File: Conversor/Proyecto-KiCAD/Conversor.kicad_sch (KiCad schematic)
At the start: 25 parts, among them J2 ConnPila, J3 ConnTrafoP, J4 ConnTrafoS, J5 ConnLf, J6 ConnCarga, Q1 IRFP150, Q2 IRFP150, Q3 IRFP150, Q4 IRFP150

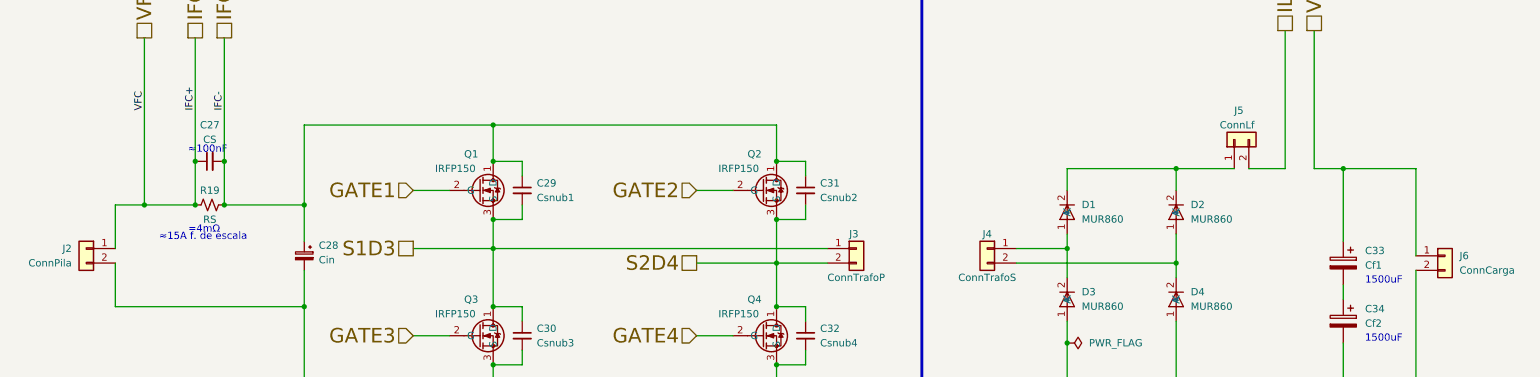
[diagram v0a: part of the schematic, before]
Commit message: Progresar con los recomendaciones de Claus
- Arreglar resistencia shunt y pistas de alimentación
- Cambiados los simbolos de conectores de trafo, pila, inductor y carga
por screw terminals, todavía no está actualizado en la PCB
- Tambien terminar de ver las layout recommendations
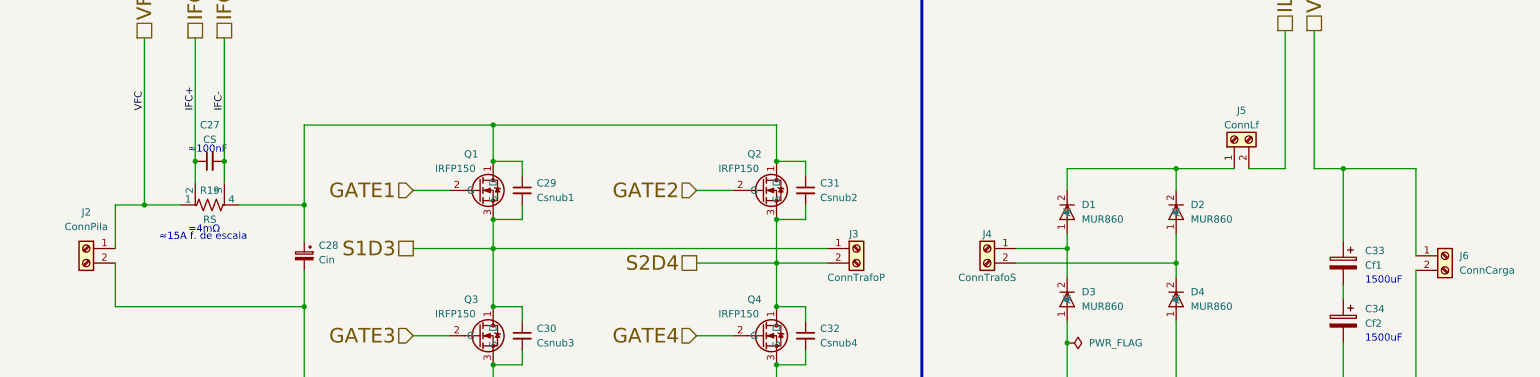
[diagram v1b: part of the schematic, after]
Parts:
- removed J2: ConnPila, TerminalBlock:TerminalBlock_Wuerth_691311400102_P7.62mm, symbol Connector_Generic:Conn_01x02
- removed J3: ConnTrafoP, TerminalBlock:TerminalBlock_Wuerth_691311400102_P7.62mm, symbol Connector_Generic:Conn_01x02
- removed J4: ConnTrafoS, TerminalBlock:TerminalBlock_Wuerth_691311400102_P7.62mm, symbol Connector_Generic:Conn_01x02
- removed J5: ConnLf, TerminalBlock:TerminalBlock_Wuerth_691311400102_P7.62mm, symbol Connector_Generic:Conn_01x02
- removed J6: ConnCarga, TerminalBlock:TerminalBlock_Wuerth_691311400102_P7.62mm, symbol Connector_Generic:Conn_01x02
- removed R19: RS, Resistor_SMD:R_2512_6332Metric_Pad1.40x3.35mm_HandSolder, symbol Device:R_Small_US
- added J2: ConnPila, symbol Connector:Screw_Terminal_01x02
- added J3: ConnTrafoP, symbol Connector:Screw_Terminal_01x02
- added J4: ConnTrafoS, symbol Connector:Screw_Terminal_01x02
- added J5: ConnLf, symbol Connector:Screw_Terminal_01x02
- added J6: ConnCarga, symbol Connector:Screw_Terminal_01x02
- added R19: RS, Resistor_SMD:R_Shunt_Vishay_WSK2512_6332Metric_T2.21mm, symbol Device:R_Shunt_US
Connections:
- net GND1: now also J2.2 (Pin_2)
- net GND2: now also J6.2 (Pin_2)
- net IFC+: now also R19.2
- net IFC-: now also R19.3; no longer C28.1, C29.1, C31.1, Q1.1 (D), Q2.1 (D)
- net ILF+: now also J5.2 (Pin_2)
- net S1D3: now also J3.1 (Pin_1)
- net S2D4: now also J3.2 (Pin_2)
- net VLOAD/ILF-: now also J6.1 (Pin_1)
- net at D1.1 (A), D3.2 (K): now also J4.1 (Pin_1)
- net at D1.2 (K), D2.2 (K): now also J5.1 (Pin_1)
- net at D2.1 (A), D4.2 (K): now also J4.2 (Pin_2)
- new net: C28.1, C29.1, C31.1, Q1.1 (D), Q2.1 (D), R19.4
- new net VFC: J2.1 (Pin_1), R19.1

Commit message: Cambiar los conectores de trafo, inductor, pila y carga
- Por hacer:
  - Cambiar el 12V HD por el conector que mostró Claus
  - Ver las layout recommendations de los reguladores lineales
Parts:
- J2, J3, J4, J5, J6: footprint (none) -> DegsonScrewTerminal:Degson_Screw_Terminal_block_01x02
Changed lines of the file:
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@@
       (effects (font (size 1.27 1.27)) (justify left))
     )
-    (property "Footprint" "" (id 2) (at 167.64 97.79 0)
+    (property "Footprint" "DegsonScrewTerminal:Degson_Screw_Terminal_block_01x02" (id 2) (at 167.64 97.79 0)
       (effects (font (size 1.27 1.27)) hide)
     )
@@
     (property "Reference" "J4" (id 0) (at 190.5 95.25 0))
     (property "Value" "ConnTrafoS" (id 1) (at 190.5 102.87 0))
-    (property "Footprint" "" (id 2) (at 190.5 97.79 0)
+    (property "Footprint" "DegsonScrewTerminal:Degson_Screw_Terminal_block_01x02" (id 2) (at 190.5 97.79 0)
       (effects (font (size 1.27 1.27)) hide)
     )
@@
     (property "Reference" "J2" (id 0) (at 33.02 91.44 0))
     (property "Value" "ConnPila" (id 1) (at 33.02 93.98 0))
-    (property "Footprint" "" (id 2) (at 33.02 97.79 0)
+    (property "Footprint" "DegsonScrewTerminal:Degson_Screw_Terminal_block_01x02" (id 2) (at 33.02 97.79 0)
       (effects (font (size 1.27 1.27)) hide)
     )
@@
       (effects (font (size 1.27 1.27)) (justify left))
     )
-    (property "Footprint" "" (id 2) (at 270.51 99.06 0)
+    (property "Footprint" "DegsonScrewTerminal:Degson_Screw_Terminal_block_01x02" (id 2) (at 270.51 99.06 0)
       (effects (font (size 1.27 1.27)) hide)
     )
@@
     (property "Reference" "J5" (id 0) (at 234.95 73.66 90))
     (property "Value" "ConnLf" (id 1) (at 234.95 76.2 90))
-    (property "Footprint" "" (id 2) (at 233.68 78.74 0)
-      (effects (font (size 1.27 1.27)) hide)
-    )
+    (property "Footprint" "DegsonScrewTerminal:Degson_Screw_Terminal_block_01x02" (id 2) (at 233.68 78.74 0)
+      (effects (font (size 1.27 1.27)) hide)
+    )

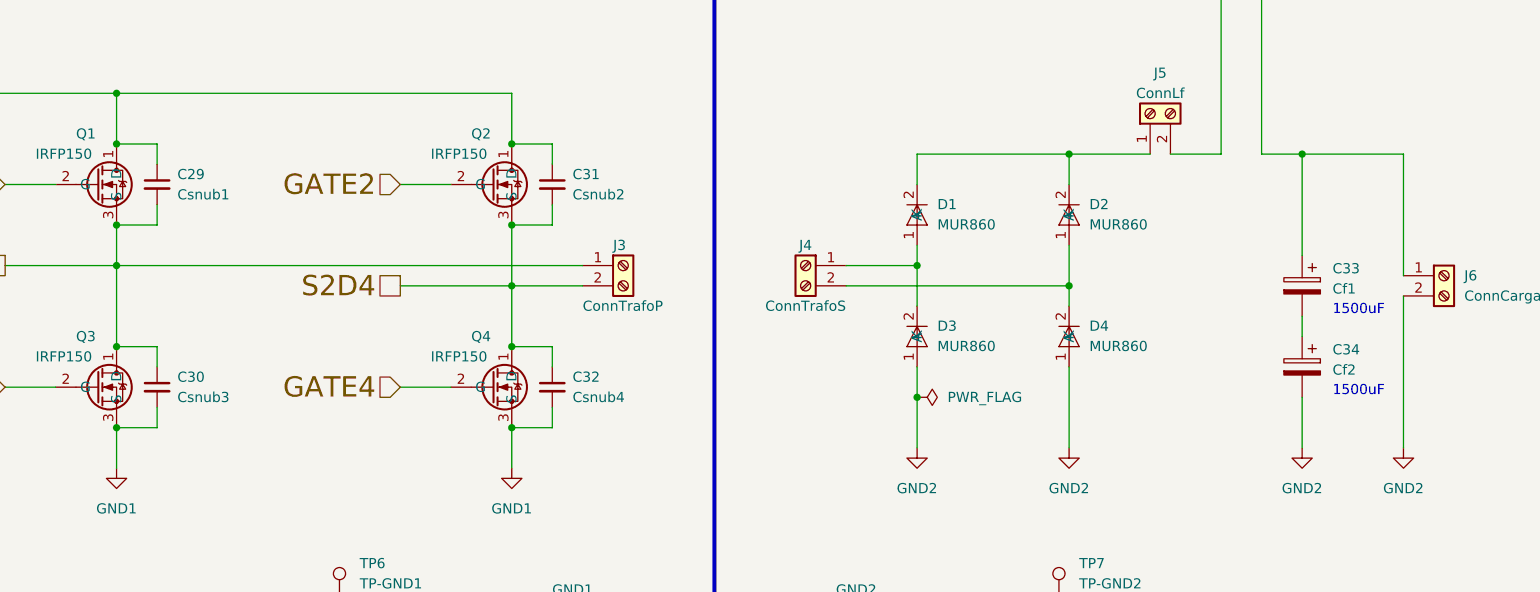
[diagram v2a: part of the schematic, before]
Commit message: Empezar con lar recomendaciones de Jorge
- Agregar nota que contiene todas las recomendaciones (ticks en las que
ya hice)
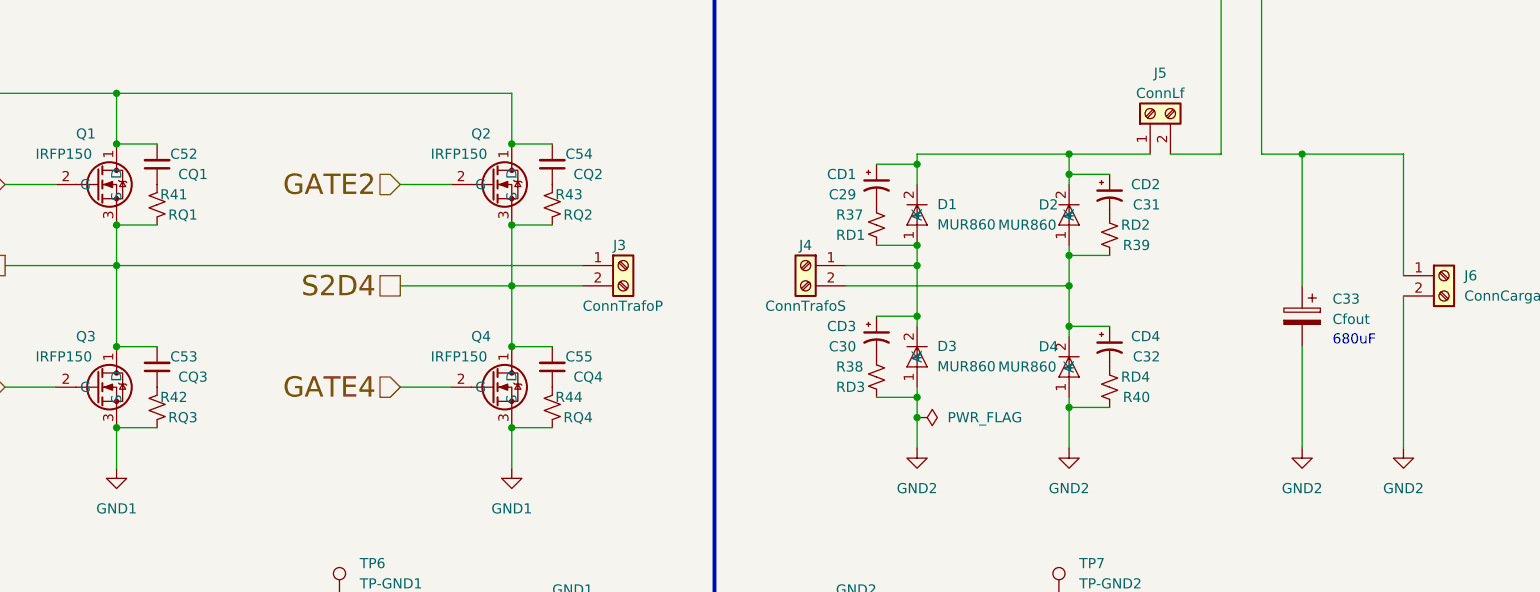
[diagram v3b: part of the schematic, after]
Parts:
- removed C29: Csnub1, Capacitor_SMD:C_1206_3216Metric_Pad1.33x1.80mm_HandSolder, symbol Device:C_Small
- removed C30: Csnub3, Capacitor_SMD:C_1206_3216Metric_Pad1.33x1.80mm_HandSolder, symbol Device:C_Small
- removed C31: Csnub2, Capacitor_SMD:C_1206_3216Metric_Pad1.33x1.80mm_HandSolder, symbol Device:C_Small
- removed C34: Cf2, Capacitor_THT:CP_Radial_D18.0mm_P7.50mm, symbol Device:C_Polarized
- added C30: CD3, Capacitor_THT:CP_Radial_Tantal_D4.5mm_P2.50mm, symbol Device:C_Polarized_Small_US
- added C31: CD2, Capacitor_THT:CP_Radial_Tantal_D4.5mm_P2.50mm, symbol Device:C_Polarized_Small_US
- added C32: CD4, Capacitor_THT:CP_Radial_Tantal_D4.5mm_P2.50mm, symbol Device:C_Polarized_Small_US
- added C52: CQ1, Capacitor_SMD:C_1206_3216Metric_Pad1.33x1.80mm_HandSolder, symbol Device:C_Small
- added C53: CQ3, Capacitor_SMD:C_1206_3216Metric_Pad1.33x1.80mm_HandSolder, symbol Device:C_Small
- added C54: CQ2, Capacitor_SMD:C_1206_3216Metric_Pad1.33x1.80mm_HandSolder, symbol Device:C_Small
- added C55: CQ4, Capacitor_SMD:C_1206_3216Metric_Pad1.33x1.80mm_HandSolder, symbol Device:C_Small
- added R37: RD1, Resistor_THT:R_Axial_DIN0204_L3.6mm_D1.6mm_P5.08mm_Horizontal, symbol Device:R_Small_US
- added R38: RD3, Resistor_THT:R_Axial_DIN0204_L3.6mm_D1.6mm_P5.08mm_Horizontal, symbol Device:R_Small_US
- added R39: RD2, Resistor_THT:R_Axial_DIN0204_L3.6mm_D1.6mm_P5.08mm_Horizontal, symbol Device:R_Small_US
- added R40: RD4, Resistor_THT:R_Axial_DIN0204_L3.6mm_D1.6mm_P5.08mm_Horizontal, symbol Device:R_Small_US
- added R41: RQ1, Resistor_SMD:R_1206_3216Metric_Pad1.30x1.75mm_HandSolder, symbol Device:R_Small_US
- added R42: RQ3, Resistor_SMD:R_1206_3216Metric_Pad1.30x1.75mm_HandSolder, symbol Device:R_Small_US
- added R43: RQ2, Resistor_SMD:R_1206_3216Metric_Pad1.30x1.75mm_HandSolder, symbol Device:R_Small_US
- added R44: RQ4, Resistor_SMD:R_1206_3216Metric_Pad1.30x1.75mm_HandSolder, symbol Device:R_Small_US
- C29: renamed from C32; value Csnub4 -> CD1; footprint Capacitor_SMD:C_1206_3216Metric_Pad1.33x1.80mm_HandSolder -> Capacitor_THT:CP_Radial_Tantal_D4.5mm_P2.50mm; symbol Device:C_Small -> Device:C_Polarized_Small_US
- C33: value Cf1 -> Cfout; footprint Capacitor_THT:CP_Radial_D18.0mm_P7.50mm -> Capacitor_THT:CP_Radial_D22.0mm_P10.00mm_SnapIn
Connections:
- net GND1: now also R42.1, R44.1; no longer C29.2
- net GND2: now also C33.2, R38.1, R40.2
- net S1D3: now also C53.2, R41.1
- net S2D4: now also C55.2, R43.1; no longer C29.1
- net at C28.1, Q1.1 (D), Q2.1 (D)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: now also C52.2, C54.2
- net at D1.1 (A), D3.2 (K), J4.1 (Pin_1): now also C30.1, R37.1
- net at D2.1 (A), D4.2 (K), J4.2 (Pin_2): now also C32.1, R39.2
- net at D1.2 (K), D2.2 (K), J5.1 (Pin_1): now also C29.1, C31.1
- new net: C30.2, R38.2
- new net: C29.2, R37.2
- new net: C55.1, R44.2
- new net: C53.1, R42.2
- new net: C52.1, R41.2
- new net: C54.1, R43.2
- new net: C31.2, R39.1
- new net: C32.2, R40.1
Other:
- note added: "680uF"
- note removed: "1500uF"
- moved on the sheet: C33, D3, D4

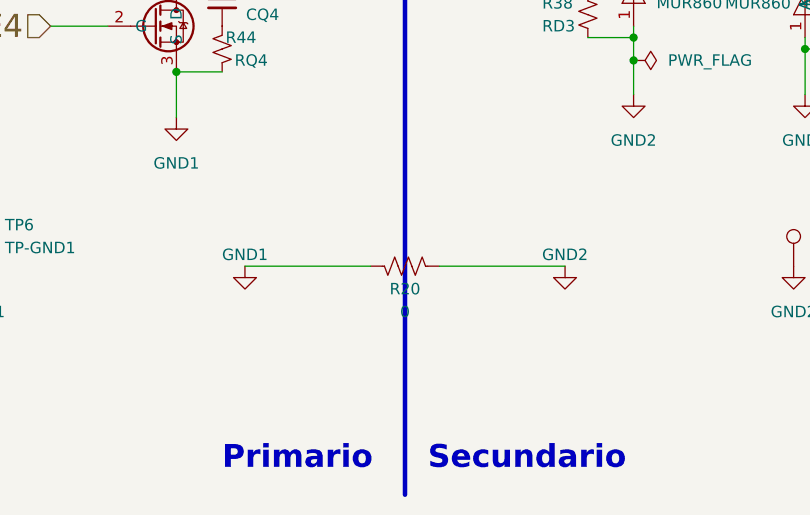
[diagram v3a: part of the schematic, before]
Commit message: Corregir las cosas que me indico Jorge
- Por hacer:
  - Verificar las correcciones con Jorge
  - Ver si se consigue un capacitor mas chico (~20mm) para la entrada
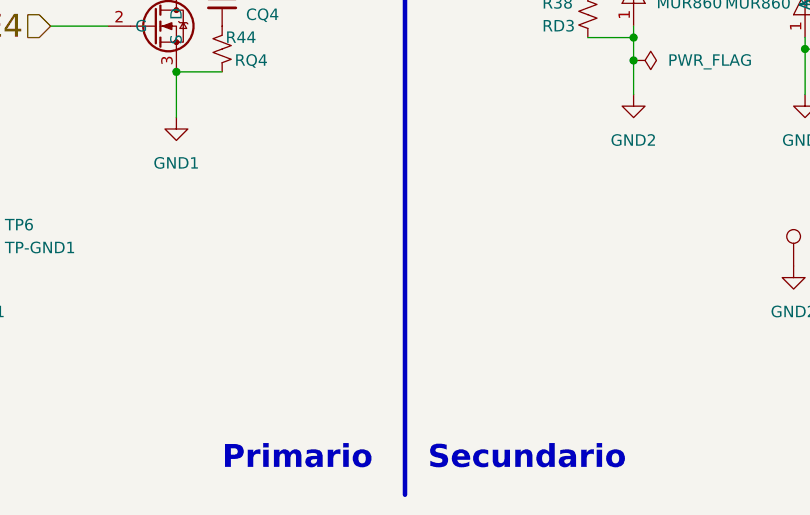
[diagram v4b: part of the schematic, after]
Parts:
- removed R20: 0, Resistor_SMD:R_1206_3216Metric_Pad1.30x1.75mm_HandSolder, symbol Device:R_US
- C28: footprint Capacitor_THT:CP_Radial_D12.5mm_P5.00mm -> Capacitor_THT:CP_Radial_D22.0mm_P10.00mm_SnapIn
- C33: footprint Capacitor_THT:CP_Radial_D22.0mm_P10.00mm_SnapIn -> Capacitor_THT:CP_Radial_D25.0mm_P10.00mm_SnapIn
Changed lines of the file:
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@@
-    (stroke (width 0) (type default) (color 0 0 0 0))
-  )
-  (wire (pts (xy 175.26 139.7) (xy 161.29 139.7))
     (stroke (width 0) (type default) (color 0 0 0 0))
   )
@@
   )
   (wire (pts (xy 204.47 116.84) (xy 204.47 120.65))
-    (stroke (width 0) (type default) (color 0 0 0 0))
-  )
-  (wire (pts (xy 196.85 139.7) (xy 182.88 139.7))
     (stroke (width 0) (type default) (color 0 0 0 0))
   )
@@
       (effects (font (size 1.27 1.27)) (justify right))
     )
-    (property "Footprint" "Capacitor_THT:CP_Radial_D12.5mm_P5.00mm" (id 2) (at 71.12 99.06 0)
+    (property "Footprint" "Capacitor_THT:CP_Radial_D22.0mm_P10.00mm_SnapIn" (id 2) (at 71.12 99.06 0)
       (effects (font (size 1.27 1.27)) hide)
     )
@@
     )
     (property "Datasheet" "" (id 3) (at 204.47 92.71 0)
-      (effects (font (size 1.27 1.27)) hide)
-    )
-    (pin "1")
-    (pin "2")
-  )
-  (symbol (lib_id "Device:R_US") (at 179.07 139.7 270) (mirror x) (unit 1)
-    (in_bom yes) (on_board yes)
-    (property "Reference" "R20" (id 0) (at 179.07 142.24 90))
-    (property "Value" "0" (id 1) (at 179.07 144.78 90))
-    (property "Footprint" "Resistor_SMD:R_1206_3216Metric_Pad1.30x1.75mm_HandSolder" (id 2) (at 178.816 138.684 90)
-      (effects (font (size 1.27 1.27)) hide)
-    )
-    (property "Datasheet" "~" (id 3) (at 179.07 139.7 0)
       (effects (font (size 1.27 1.27)) hide)
     )
@@
     (pin "1")
   )
-  (symbol (lib_id "power:GND1") (at 161.29 139.7 0) (mirror y) (unit 1)
-    (in_bom yes) (on_board yes)
-    (property "Reference" "#PWR069" (id 0) (at 161.29 146.05 0)
-      (effects (font (size 1.27 1.27)) hide)
-    )
-    (property "Value" "GND1" (id 1) (at 161.29 138.43 0))
-    (property "Footprint" "" (id 2) (at 161.29 139.7 0)
-      (effects (font (size 1.27 1.27)) hide)
-    )
-    (property "Datasheet" "" (id 3) (at 161.29 139.7 0)
-      (effects (font (size 1.27 1.27)) hide)
-    )
-    (pin "1")
-  )
   (symbol (lib_id "power:GND2") (at 204.47 120.65 0) (unit 1)
     (in_bom yes) (on_board yes) (fields_autoplaced)
@@
     )
     (property "Datasheet" "" (id 3) (at 204.47 120.65 0)
-      (effects (font (size 1.27 1.27)) hide)
-    )
-    (pin "1")
-  )
-  (symbol (lib_id "power:GND2") (at 196.85 139.7 0) (mirror y) (unit 1)
-    (in_bom yes) (on_board yes)
-    (property "Reference" "#PWR070" (id 0) (at 196.85 146.05 0)
-      (effects (font (size 1.27 1.27)) hide)
-    )
-    (property "Value" "GND2" (id 1) (at 196.85 138.43 0))
-    (property "Footprint" "" (id 2) (at 196.85 139.7 0)
-      (effects (font (size 1.27 1.27)) hide)
-    )
-    (property "Datasheet" "" (id 3) (at 196.85 139.7 0)
       (effects (font (size 1.27 1.27)) hide)
     )
@@
       (effects (font (size 1.27 1.27)) (justify right))
     )
-    (property "Footprint" "Capacitor_THT:CP_Radial_D22.0mm_P10.00mm_SnapIn" (id 2) (at 251.7648 107.95 0)
-      (effects (font (size 1.27 1.27)) hide)
-    )
+    (property "Footprint" "Capacitor_THT:CP_Radial_D25.0mm_P10.00mm_SnapIn" (id 2) (at 251.7648 107.95 0)
+      (effects (font (size 1.27 1.27)) hide)
+    )

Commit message: Seguir emprolijando la plaqueta
- Rehacer el layout de resistencias de pull-up del lado primario
- Mover el LM5056 mas arriba para permitir que entre el capacitor de 25mm de diametro
- Cambiar cosas para seguir las layout recommendations de componentes:
  - Sacar todo el cobre de abajo del ISO7242M y re-rutear acordemente
  - Reorganizar las R y C del Op-Amp según indica la hoja de datos
Por hacer:
  - Últimas verificaciones y ya mandar mail a MayerPCB para ir cotizando todo (cotización lista en una semana?)
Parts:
- C28: footprint Capacitor_THT:CP_Radial_D22.0mm_P10.00mm_SnapIn -> Capacitor_THT:CP_Radial_D25.0mm_P10.00mm_SnapIn
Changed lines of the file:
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@@
       (effects (font (size 1.27 1.27)) (justify right))
     )
-    (property "Footprint" "Capacitor_THT:CP_Radial_D22.0mm_P10.00mm_SnapIn" (id 2) (at 71.12 99.06 0)
+    (property "Footprint" "Capacitor_THT:CP_Radial_D25.0mm_P10.00mm_SnapIn" (id 2) (at 71.12 99.06 0)
       (effects (font (size 1.27 1.27)) hide)
     )
